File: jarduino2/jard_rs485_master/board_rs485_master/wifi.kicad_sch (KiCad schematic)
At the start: 3 parts, among them U5 BPC_ESP8266-01_ESP-01

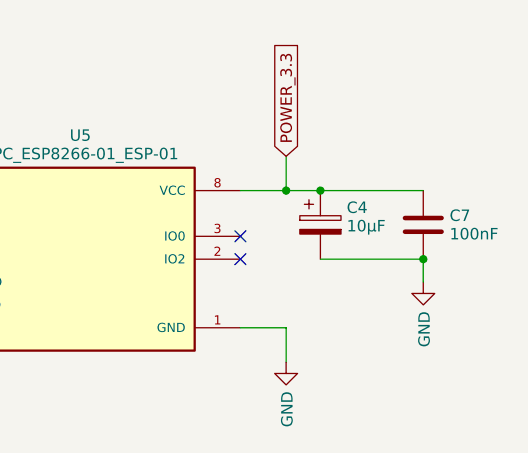
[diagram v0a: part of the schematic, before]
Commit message: Candidate pour revue du master Oyas (avec modules en tant que shield MEGA)
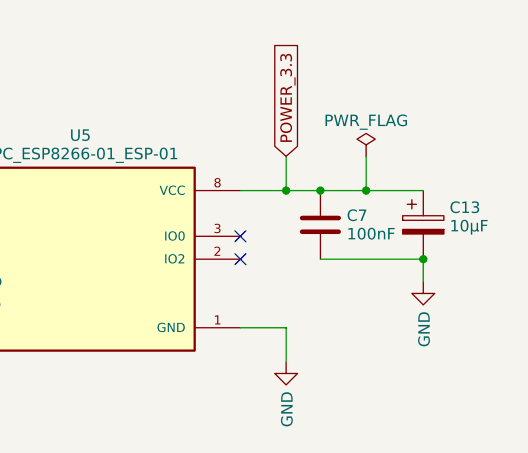
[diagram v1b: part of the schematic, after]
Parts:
- removed C4: 10µF, Capacitor_THT:CP_Radial_D4.0mm_P2.00mm, symbol Device:C_Polarized
- added C13: 10µF, Capacitor_THT:CP_Radial_D4.0mm_P2.00mm, symbol Device:C_Polarized
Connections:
- net GND: now also C13.2
- net POWER_3.3: now also C13.1
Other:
- company: (none) -> BPC
- title: (none) -> Commande des OYA - Maître RS485
- moved on the sheet: C7
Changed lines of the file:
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@@
 (kicad_sch (version 20230121) (generator eeschema)
   (paper "A4")
+  (title_block
+    (title "Commande des OYA - Maître RS485")
+    (date "2024-03-30")
+    (rev "A0")
+    (company "BPC")
+    (comment 1 "Extension Wifi (ESP01)")
+    (comment 2 "Inteface LEDs RGB - Bouton - RTC")
+    (comment 3 "Alim 12V - Sortie 12V pilotable - Bus RS485")
+  )
   (junction (at 147.32 90.17) (diameter 0) (color 0 0 0 0)
   )
@@
   )
   (junction (at 162.56 97.79) (diameter 0) (color 0 0 0 0)
+  )
+  (junction (at 156.21 90.17) (diameter 0) (color 0 0 0 0)
   )
   (no_connect (at 142.24 95.25))
@@
   (no_connect (at 106.68 92.71))
   (no_connect (at 142.24 97.79))
+  (wire (pts (xy 151.13 90.17) (xy 156.21 90.17))
+    (stroke (width 0) (type default))
+  )
   (wire (pts (xy 147.32 90.17) (xy 151.13 90.17))
     (stroke (width 0) (type default))
   )
-  (wire (pts (xy 151.13 90.17) (xy 162.56 90.17))
-    (stroke (width 0) (type default))
-  )
   (wire (pts (xy 142.24 105.41) (xy 147.32 105.41))
     (stroke (width 0) (type default))
@@
     (stroke (width 0) (type default))
   )
+  (wire (pts (xy 156.21 90.17) (xy 162.56 90.17))
+    (stroke (width 0) (type default))
+  )
   (wire (pts (xy 162.56 97.79) (xy 162.56 100.33))
     (stroke (width 0) (type default))
   )
   (wire (pts (xy 147.32 105.41) (xy 147.32 109.22))
+    (stroke (width 0) (type default))
+  )
+  (wire (pts (xy 156.21 86.36) (xy 156.21 90.17))
     (stroke (width 0) (type default))
   )
@@
     )
   )
-  (symbol (lib_id "Device:C_Polarized") (at 151.13 93.98 0) (unit 1)
-    (in_bom yes) (on_board yes) (dnp no) (fields_autoplaced)
-    (property "Reference" "C4" (at 154.051 92.067 0)
-      (effects (font (size 1.27 1.27)) (justify left))
-    )
-    (property "Value" "10µF" (at 154.051 94.115 0)
-      (effects (font (size 1.27 1.27)) (justify left))
-    )
-    (property "Footprint" "Capacitor_THT:CP_Radial_D4.0mm_P2.00mm" (at 152.0952 97.79 0)
-      (effects (font (size 1.27 1.27)) hide)
-    )
-    (property "Datasheet" "~" (at 151.13 93.98 0)
+  (symbol (lib_id "Device:C_Polarized") (at 162.56 93.98 0) (unit 1)
+    (in_bom yes) (on_board yes) (dnp no) (fields_autoplaced)
+    (property "Reference" "C13" (at 165.481 92.067 0)
+      (effects (font (size 1.27 1.27)) (justify left))
+    )
+    (property "Value" "10µF" (at 165.481 94.115 0)
+      (effects (font (size 1.27 1.27)) (justify left))
+    )
+    (property "Footprint" "Capacitor_THT:CP_Radial_D4.0mm_P2.00mm" (at 163.5252 97.79 0)
+      (effects (font (size 1.27 1.27)) hide)
+    )
+    (property "Datasheet" "~" (at 162.56 93.98 0)
       (effects (font (size 1.27 1.27)) hide)
     )
@@
       (project "board_rs485_master"
         (path "/27904310-f1aa-47e2-a2a6-8db936442bd1/2eaa2441-998c-4f1a-b526-09e479f565d5"
-          (reference "C4") (unit 1)
+          (reference "C13") (unit 1)
         )
         (path "/27904310-f1aa-47e2-a2a6-8db936442bd1/ad7fcf36-7748-47c7-b2d8-753e3fd3e3b0"
@@
         (path "/27904310-f1aa-47e2-a2a6-8db936442bd1/41a39135-3725-490c-abfb-c5b2d926b4a7"
           (reference "C1") (unit 1)
+        )
+      )
+    )
+  )
+  (symbol (lib_id "power:PWR_FLAG") (at 156.21 86.36 0) (unit 1)
+    (in_bom yes) (on_board yes) (dnp no) (fields_autoplaced)
+    (property "Reference" "#FLG02" (at 156.21 84.455 0)
+      (effects (font (size 1.27 1.27)) hide)
+    )
+    (property "Value" "PWR_FLAG" (at 156.21 82.415 0)
+      (effects (font (size 1.27 1.27)))
+    )
+    (property "Footprint" "" (at 156.21 86.36 0)
+      (effects (font (size 1.27 1.27)) hide)
+    )
+    (property "Datasheet" "~" (at 156.21 86.36 0)
+      (effects (font (size 1.27 1.27)) hide)
+    )
+    (pin "1")
+    (instances
+      (project "board_rs485_master"
+        (path "/27904310-f1aa-47e2-a2a6-8db936442bd1/41a39135-3725-490c-abfb-c5b2d926b4a7"
+          (reference "#FLG02") (unit 1)
         )
       )
@@
     )
   )
-  (symbol (lib_id "Device:C") (at 162.56 93.98 0) (unit 1)
-    (in_bom yes) (on_board yes) (dnp no) (fields_autoplaced)
-    (property "Reference" "C7" (at 165.481 92.956 0)
-      (effects (font (size 1.27 1.27)) (justify left))
-    )
-    (property "Value" "100nF" (at 165.481 95.004 0)
-      (effects (font (size 1.27 1.27)) (justify left))
-    )
-    (property "Footprint" "Capacitor_THT:C_Disc_D5.0mm_W2.5mm_P2.50mm" (at 163.5252 97.79 0)
-      (effects (font (size 1.27 1.27)) hide)
-    )
-    (property "Datasheet" "~" (at 162.56 93.98 0)
-      (effects (font (size 1.27 1.27)) hide)
-    )
+  (symbol (lib_id "Device:C") (at 151.13 93.98 0) (unit 1)
+    (in_bom yes) (on_board yes) (dnp no) (fields_autoplaced)
+    (property "Reference" "C7" (at 154.051 92.956 0)
+      (effects (font (size 1.27 1.27)) (justify left))
+    )
+    (property "Value" "100nF" (at 154.051 95.004 0)
+      (effects (font (size 1.27 1.27)) (justify left))
+    )
+    (property "Footprint" "Capacitor_THT:C_Disc_D5.0mm_W2.5mm_P2.50mm" (at 152.0952 97.79 0)
+      (effects (font (size 1.27 1.27)) hide)
+    )
+    (property "Datasheet" "~" (at 151.13 93.98 0)
+      (effects (font (size 1.27 1.27)) hide)
+    )

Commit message: Finalisation dossier
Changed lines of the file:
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@@
   (title_block
     (title "Commande des OYA - Maître RS485")
-    (date "2024-03-30")
+    (date "2024-03-31")
     (rev "A0")
     (company "BPC")
@@
   (junction (at 162.56 97.79) (diameter 0) (color 0 0 0 0)
   )
-  (junction (at 156.21 90.17) (diameter 0) (color 0 0 0 0)
-  )
   (no_connect (at 142.24 95.25))
   (no_connect (at 106.68 95.25))
   (no_connect (at 106.68 92.71))
   (no_connect (at 142.24 97.79))
-  (wire (pts (xy 151.13 90.17) (xy 156.21 90.17))
-    (stroke (width 0) (type default))
-  )
   (wire (pts (xy 147.32 90.17) (xy 151.13 90.17))
     (stroke (width 0) (type default))
@@
     (stroke (width 0) (type default))
   )
-  (wire (pts (xy 156.21 90.17) (xy 162.56 90.17))
+  (wire (pts (xy 151.13 90.17) (xy 162.56 90.17))
     (stroke (width 0) (type default))
   )
@@
   )
   (wire (pts (xy 147.32 105.41) (xy 147.32 109.22))
-    (stroke (width 0) (type default))
-  )
-  (wire (pts (xy 156.21 86.36) (xy 156.21 90.17))
     (stroke (width 0) (type default))
   )
@@
         )
       )
-    )
-  )
-  (symbol (lib_id "power:PWR_FLAG") (at 156.21 86.36 0) (unit 1)
-    (in_bom yes) (on_board yes) (dnp no) (fields_autoplaced)
-    (property "Reference" "#FLG02" (at 156.21 84.455 0)
-      (effects (font (size 1.27 1.27)) hide)
-    )
-    (property "Value" "PWR_FLAG" (at 156.21 82.415 0)
-      (effects (font (size 1.27 1.27)))
-    )
-    (property "Footprint" "" (at 156.21 86.36 0)
-      (effects (font (size 1.27 1.27)) hide)
-    )
-    (property "Datasheet" "~" (at 156.21 86.36 0)
-      (effects (font (size 1.27 1.27)) hide)
-    )
-    (pin "1")
-    (instances
-      (project "board_rs485_master"
-        (path "/27904310-f1aa-47e2-a2a6-8db936442bd1/41a39135-3725-490c-abfb-c5b2d926b4a7"
-          (reference "#FLG02") (unit 1)
-        )
-      )

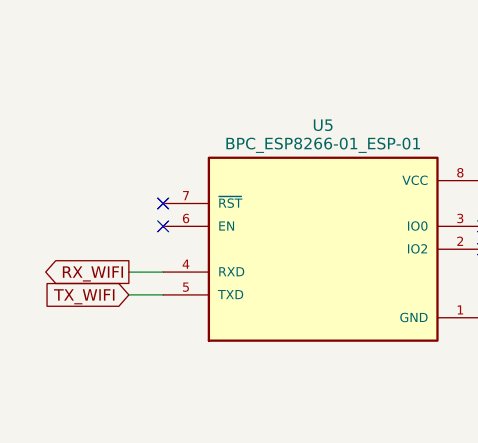
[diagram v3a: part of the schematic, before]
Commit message: Correction de l'inversion RX/TX du module Wifi
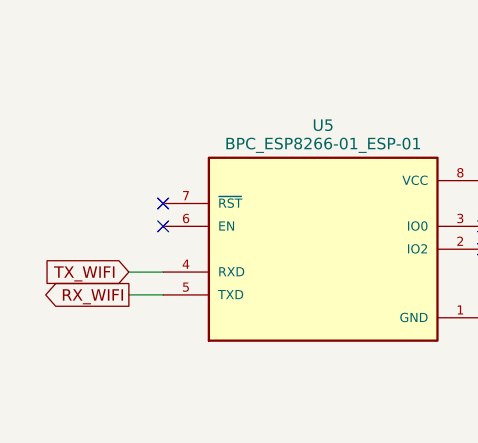
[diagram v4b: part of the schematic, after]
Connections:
- net RX_WIFI: now also U5.5 (TXD); no longer U5.4 (RXD)
- net TX_WIFI: now also U5.4 (RXD); no longer U5.5 (TXD)
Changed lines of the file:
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@@
   (title_block
     (title "Commande des OYA - Maître RS485")
-    (date "2024-04-09")
+    (date "2024-04-24")
     (rev "B0")
     (company "BPC")
@@
   (no_connect (at 106.68 92.71))
   (no_connect (at 142.24 97.79))
+  (wire (pts (xy 102.87 100.33) (xy 106.68 100.33))
+    (stroke (width 0) (type default))
+  )
   (wire (pts (xy 147.32 90.17) (xy 151.13 90.17))
     (stroke (width 0) (type default))
@@
     (stroke (width 0) (type default))
   )
-  (wire (pts (xy 102.87 100.33) (xy 106.68 100.33))
-    (stroke (width 0) (type default))
-  )
   (wire (pts (xy 147.32 90.17) (xy 147.32 86.36))
     (stroke (width 0) (type default))
   )
-  (global_label "TX_WIFI" (shape input) (at 102.87 102.87 180) (fields_autoplaced)
+  (global_label "TX_WIFI" (shape input) (at 102.87 100.33 180) (fields_autoplaced)
     (effects (font (size 1.27 1.27)) (justify right))
-    (property "Intersheetrefs" "${INTERSHEET_REFS}" (at 93.7241 102.87 0)
+    (property "Intersheetrefs" "${INTERSHEET_REFS}" (at 93.7241 100.33 0)
       (effects (font (size 1.27 1.27)) (justify right) hide)
     )
@@
     )
   )
-  (global_label "RX_WIFI" (shape output) (at 102.87 100.33 180) (fields_autoplaced)
+  (global_label "RX_WIFI" (shape output) (at 102.87 102.87 180) (fields_autoplaced)
     (effects (font (size 1.27 1.27)) (justify right))
-    (property "Intersheetrefs" "${INTERSHEET_REFS}" (at 93.4217 100.33 0)
+    (property "Intersheetrefs" "${INTERSHEET_REFS}" (at 93.4217 102.87 0)
       (effects (font (size 1.27 1.27)) (justify right) hide)
     )

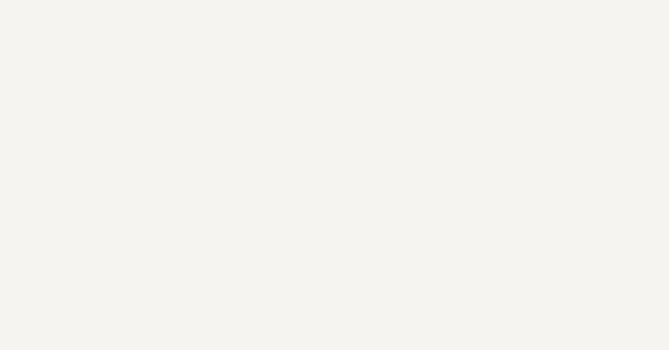
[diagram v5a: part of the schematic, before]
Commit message: Titres + finitions (vias)
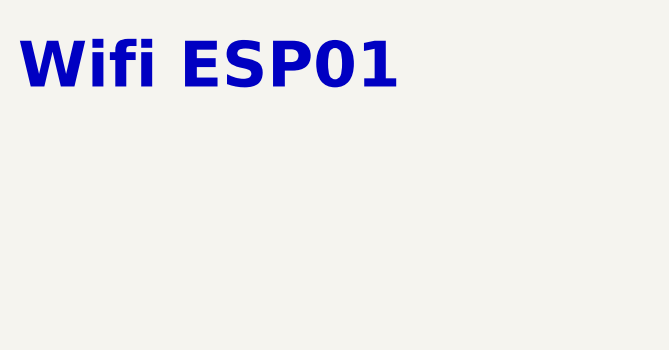
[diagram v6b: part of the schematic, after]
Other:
- note added: "Wifi ESP01"
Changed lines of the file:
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@@
     (stroke (width 0) (type default))
+  )
+  (text "Wifi ESP01" (at 19.05 27.94 0)
+    (effects (font (size 5.08 5.08) (thickness 2.54) bold) (justify left bottom))
   )
   (global_label "TX_WIFI" (shape input) (at 102.87 100.33 180) (fields_autoplaced)
